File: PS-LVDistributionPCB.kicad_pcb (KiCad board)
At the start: 2 copper layers, 166.5 x 58.5 mm, 41 parts, among them J1 Conn_01x02, J10 Conn_01x02, J11 Conn_01x02, J12 Conn_01x02, J13 Conn_01x02, J14 Conn_01x02, J15 Conn_01x20, J2 Conn_01x02, J3 Conn_01x02, J4 Conn_01x02, J5 Conn_01x02, J6 Conn_01x02, J7 Conn_01x02, J8 Conn_01x02, J9 Conn_01x02

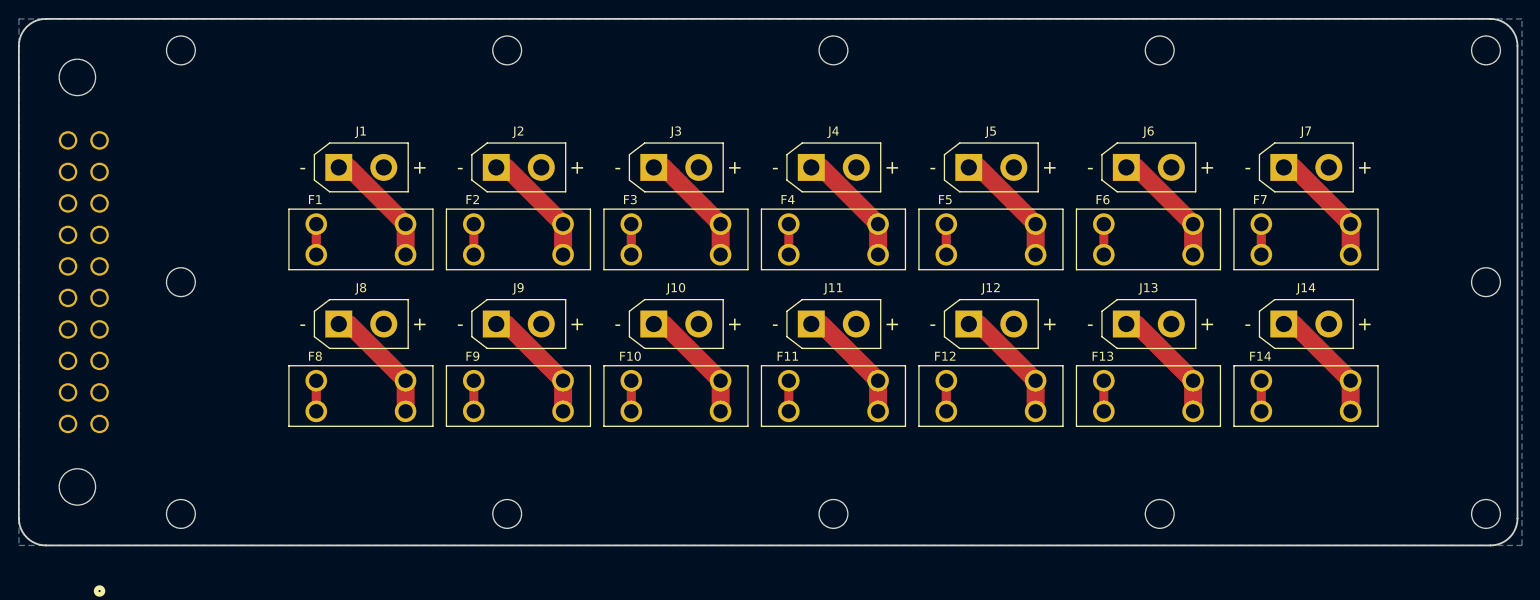
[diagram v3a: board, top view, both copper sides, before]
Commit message: removed 2 outputs + smaller
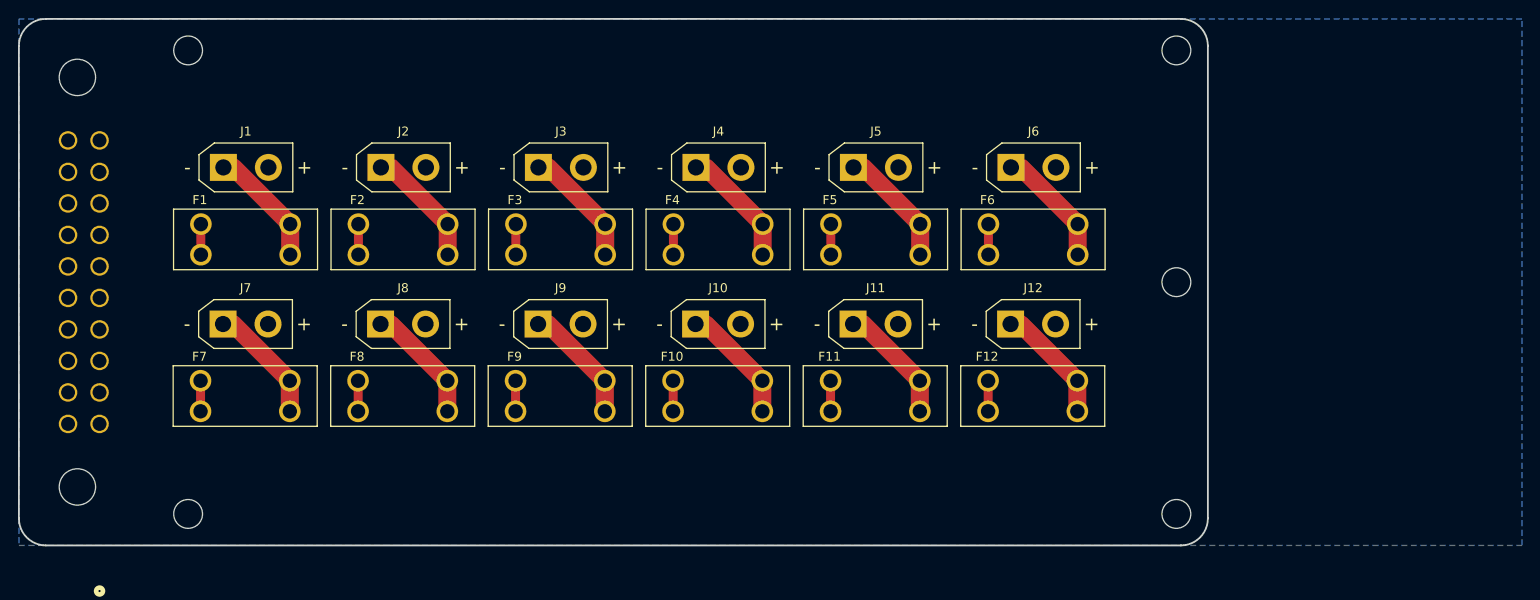
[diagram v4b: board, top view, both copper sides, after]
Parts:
- removed F13, F14: 3568, footprints:FUSE_3568
- removed J13, J14: Conn_01x02, footprints:AMASS_XT30UPB-M_1x02_P5.0mm_Vertical
- removed the REF** at (104.0, 87.2)
- removed the REF** at (176.5, 61.5)
- removed the REF** at (176.5, 113.0)
- removed the REF** at (104.0, 61.5)
- removed the REF** at (212.8, 113.0)
- removed the REF** at (212.8, 61.5)
- removed the REF** at (104.0, 113.0)
- moved F7 119.1 mm to (111.1, 99.9)
- moved J7 119.1 mm to (108.7, 91.9)
- moved REF** 35.5 mm to (104.8, 113.0)
- moved REF** 35.5 mm to (104.8, 61.5)
- moved REF** 34.4 mm to (214.6, 87.2)
- moved REF** 34.4 mm to (214.6, 113.0)
- moved REF** 34.4 mm to (214.6, 61.5)
- moved J1 12.8 mm to (108.7, 74.5)
- moved F1 12.8 mm to (111.2, 82.5)
- moved F2 12.8 mm to (128.7, 82.5)
- moved F3 12.8 mm to (146.2, 82.5)
- moved F4 12.8 mm to (163.7, 82.5)
- moved F5 12.8 mm to (181.2, 82.5)
- moved F6 12.8 mm to (198.7, 82.5)
- moved J2 12.8 mm to (126.2, 74.5)
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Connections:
- J15 pad 13: P13 -> GND
- J15 pad 14: P14 -> GND
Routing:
- net Net-(J14-Pin_1): track 13.4 -> 0.00 mm
- net Net-(J13-Pin_1): track 13.4 -> 0.00 mm
- net P14: track 3.40 -> 0.00 mm
- net P13: track 3.40 -> 0.00 mm
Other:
- board size 166.5 x 58.5 mm -> 132.1 x 58.5 mm
